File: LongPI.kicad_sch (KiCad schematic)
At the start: 10 parts, among them J1 USB_C_Receptacle_USB2.0, J2 Conn_01x30, U1 RP2040, U2 USBLC6-2SC6, U3 XC6210B332MR, U4 W25Q128JVS

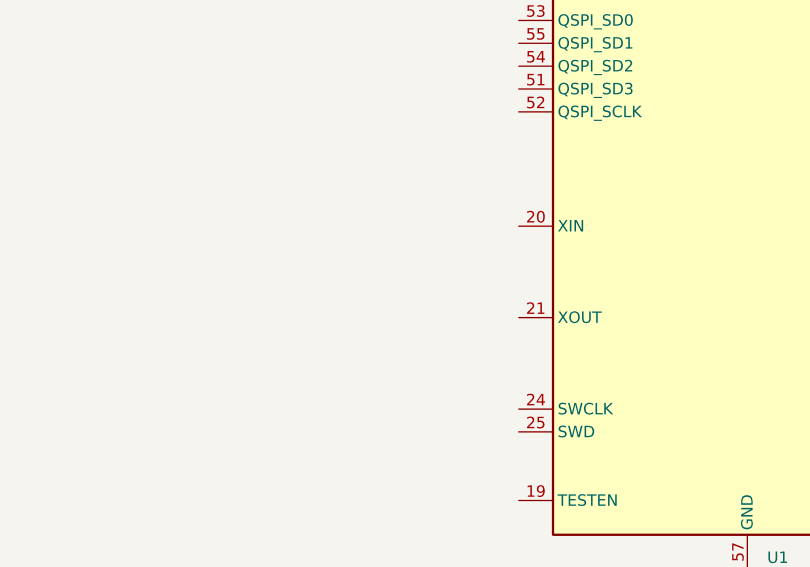
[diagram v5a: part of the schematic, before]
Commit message: Crystal setup on sch
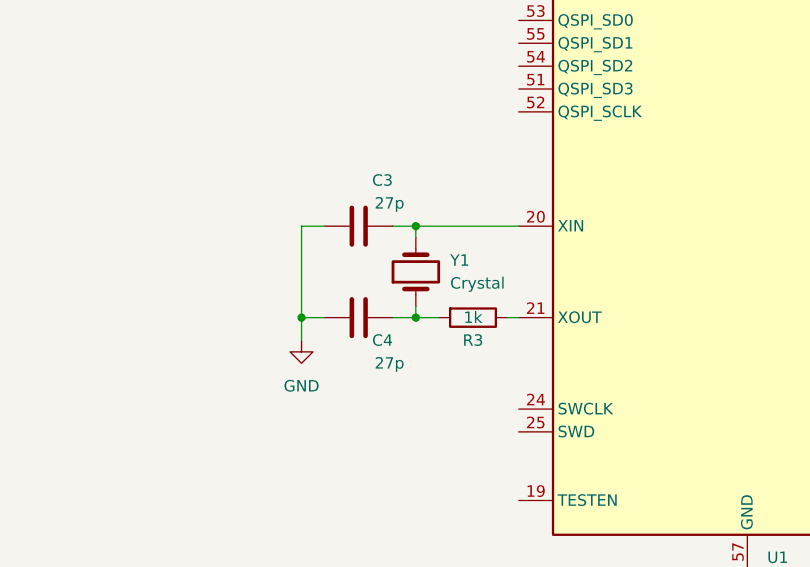
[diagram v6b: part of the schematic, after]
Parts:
- added C3, C4: 27p, symbol Device:C
- added R3: 1k, symbol Device:R
- added Y1: Crystal, symbol Device:Crystal
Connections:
- net GND: now also C3.1, C4.1
- net at U1.20 (XIN): now also C3.2, Y1.2
- net at U1.21 (XOUT): now also R3.1
- new net: C4.2, R3.2, Y1.1
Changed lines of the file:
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@@
   (junction (at 25.4 85.09) (diameter 0) (color 0 0 0 0)
   )
+  (junction (at 151.13 82.55) (diameter 0) (color 0 0 0 0)
+  )
   (junction (at 53.34 39.37) (diameter 0) (color 0 0 0 0)
   )
@@
   (junction (at 35.56 63.5) (diameter 0) (color 0 0 0 0)
   )
+  (junction (at 151.13 72.39) (diameter 0) (color 0 0 0 0)
+  )
   (junction (at 25.4 90.17) (diameter 0) (color 0 0 0 0)
   )
   (junction (at 53.34 85.09) (diameter 0) (color 0 0 0 0)
+  )
+  (junction (at 138.43 82.55) (diameter 0) (color 0 0 0 0)
   )
   (junction (at 93.98 121.92) (diameter 0) (color 0 0 0 0)
@@
     (stroke (width 0) (type default))
   )
+  (wire (pts (xy 138.43 72.39) (xy 138.43 82.55))
+    (stroke (width 0) (type default))
+  )
+  (wire (pts (xy 140.97 82.55) (xy 138.43 82.55))
+    (stroke (width 0) (type default))
+  )
   (wire (pts (xy 71.12 31.75) (xy 71.12 34.29))
     (stroke (width 0) (type default))
@@
     (stroke (width 0) (type default))
   )
+  (wire (pts (xy 151.13 82.55) (xy 151.13 81.28))
+    (stroke (width 0) (type default))
+  )
+  (wire (pts (xy 151.13 72.39) (xy 162.56 72.39))
+    (stroke (width 0) (type default))
+  )
   (wire (pts (xy 53.34 41.91) (xy 55.88 41.91))
     (stroke (width 0) (type default))
@@
     (stroke (width 0) (type default))
   )
+  (wire (pts (xy 148.59 72.39) (xy 151.13 72.39))
+    (stroke (width 0) (type default))
+  )
   (wire (pts (xy 39.37 97.79) (xy 39.37 100.33))
     (stroke (width 0) (type default))
@@
     (stroke (width 0) (type default))
   )
+  (wire (pts (xy 151.13 72.39) (xy 151.13 73.66))
+    (stroke (width 0) (type default))
+  )
   (wire (pts (xy 25.4 100.33) (xy 25.4 99.06))
     (stroke (width 0) (type default))
@@
     (stroke (width 0) (type default))
   )
+  (wire (pts (xy 138.43 82.55) (xy 138.43 85.09))
+    (stroke (width 0) (type default))
+  )
+  (wire (pts (xy 140.97 72.39) (xy 138.43 72.39))
+    (stroke (width 0) (type default))
+  )
   (wire (pts (xy 93.98 120.65) (xy 93.98 121.92))
     (stroke (width 0) (type default))
@@
     (stroke (width 0) (type default))
   )
+  (wire (pts (xy 148.59 82.55) (xy 151.13 82.55))
+    (stroke (width 0) (type default))
+  )
   (wire (pts (xy 53.34 39.37) (xy 55.88 39.37))
     (stroke (width 0) (type default))
@@
     (stroke (width 0) (type default))
   )
+  (wire (pts (xy 151.13 82.55) (xy 153.67 82.55))
+    (stroke (width 0) (type default))
+  )
   (wire (pts (xy 81.28 130.81) (xy 83.82 130.81))
     (stroke (width 0) (type default))
@@
   )
   (wire (pts (xy 25.4 100.33) (xy 39.37 100.33))
+    (stroke (width 0) (type default))
+  )
+  (wire (pts (xy 161.29 82.55) (xy 162.56 82.55))
     (stroke (width 0) (type default))
   )
@@
         (path "/cc33761c-f139-4a76-bdf7-f72d959ddb3d"
           (reference "#PWR09") (unit 1)
+        )
+      )
+    )
+  )
+  (symbol (lib_id "Device:Crystal") (at 151.13 77.47 90) (unit 1)
+    (in_bom yes) (on_board yes) (dnp no) (fields_autoplaced)
+    (property "Reference" "Y1" (at 154.94 76.2 90)
+      (effects (font (size 1.27 1.27)) (justify right))
+    )
+    (property "Value" "Crystal" (at 154.94 78.74 90)
+      (effects (font (size 1.27 1.27)) (justify right))
+    )
+    (property "Footprint" "" (at 151.13 77.47 0)
+      (effects (font (size 1.27 1.27)) hide)
+    )
+    (property "Datasheet" "~" (at 151.13 77.47 0)
+      (effects (font (size 1.27 1.27)) hide)
+    )
+    (pin "1")
+    (pin "2")
+    (instances
+      (project "LongPI"
+        (path "/cc33761c-f139-4a76-bdf7-f72d959ddb3d"
+          (reference "Y1") (unit 1)
         )
       )
@@
     )
   )
+  (symbol (lib_id "power:GND") (at 138.43 85.09 0) (unit 1)
+    (in_bom yes) (on_board yes) (dnp no) (fields_autoplaced)
+    (property "Reference" "#PWR011" (at 138.43 91.44 0)
+      (effects (font (size 1.27 1.27)) hide)
+    )
+    (property "Value" "GND" (at 138.43 90.17 0)
+      (effects (font (size 1.27 1.27)))
+    )
+    (property "Footprint" "" (at 138.43 85.09 0)
+      (effects (font (size 1.27 1.27)) hide)
+    )
+    (property "Datasheet" "" (at 138.43 85.09 0)
+      (effects (font (size 1.27 1.27)) hide)
+    )
+    (pin "1")
+    (instances
+      (project "LongPI"
+        (path "/cc33761c-f139-4a76-bdf7-f72d959ddb3d"
+          (reference "#PWR011") (unit 1)
+        )
+      )
+    )
+  )
   (symbol (lib_id "Connector:USB_C_Receptacle_USB2.0") (at 35.56 39.37 0) (unit 1)
     (in_bom yes) (on_board yes) (dnp no) (fields_autoplaced)
@@
         (path "/cc33761c-f139-4a76-bdf7-f72d959ddb3d"
           (reference "J1") (unit 1)
+        )
+      )
+    )
+  )
+  (symbol (lib_id "Device:C") (at 144.78 82.55 90) (unit 1)
+    (in_bom yes) (on_board yes) (dnp no)
+    (property "Reference" "C4" (at 148.59 85.09 90)
+      (effects (font (size 1.27 1.27)) (justify left))
+    )
+    (property "Value" "27p" (at 149.86 87.63 90)
+      (effects (font (size 1.27 1.27)) (justify left))
+    )
+    (property "Footprint" "" (at 148.59 81.5848 0)
+      (effects (font (size 1.27 1.27)) hide)
+    )
+    (property "Datasheet" "~" (at 144.78 82.55 0)
+      (effects (font (size 1.27 1.27)) hide)
+    )
+    (pin "1")
+    (pin "2")
+    (instances
+      (project "LongPI"
+        (path "/cc33761c-f139-4a76-bdf7-f72d959ddb3d"
+          (reference "C4") (unit 1)
+        )
+      )
+    )
+  )
+  (symbol (lib_id "Device:R") (at 157.48 82.55 270) (unit 1)
+    (in_bom yes) (on_board yes) (dnp no)
+    (property "Reference" "R3" (at 157.48 85.09 90)
+      (effects (font (size 1.27 1.27)))
+    )
+    (property "Value" "1k" (at 157.48 82.55 90)
+      (effects (font (size 1.27 1.27)))
+    )
+    (property "Footprint" "" (at 157.48 80.772 90)
+      (effects (font (size 1.27 1.27)) hide)
+    )
+    (property "Datasheet" "~" (at 157.48 82.55 0)
+      (effects (font (size 1.27 1.27)) hide)
+    )
+    (pin "1")
+    (pin "2")
+    (instances
+      (project "LongPI"
+        (path "/cc33761c-f139-4a76-bdf7-f72d959ddb3d"
+          (reference "R3") (unit 1)
         )
       )
@@
         )
       )
+    )
+  )
+  (symbol (lib_id "Device:C") (at 144.78 72.39 90) (unit 1)
+    (in_bom yes) (on_board yes) (dnp no)
+    (property "Reference" "C3" (at 148.59 67.31 90)
+      (effects (font (size 1.27 1.27)) (justify left))
+    )
+    (property "Value" "27p" (at 149.86 69.85 90)
+      (effects (font (size 1.27 1.27)) (justify left))
+    )
+    (property "Footprint" "" (at 148.59 71.4248 0)
+      (effects (font (size 1.27 1.27)) hide)
+    )
+    (property "Datasheet" "~" (at 144.78 72.39 0)
+      (effects (font (size 1.27 1.27)) hide)
+    )
+    (pin "1")
+    (pin "2")
+    (instances
+      (project "LongPI"
+        (path "/cc33761c-f139-4a76-bdf7-f72d959ddb3d"
+          (reference "C3") (unit 1)
+        )
+      )

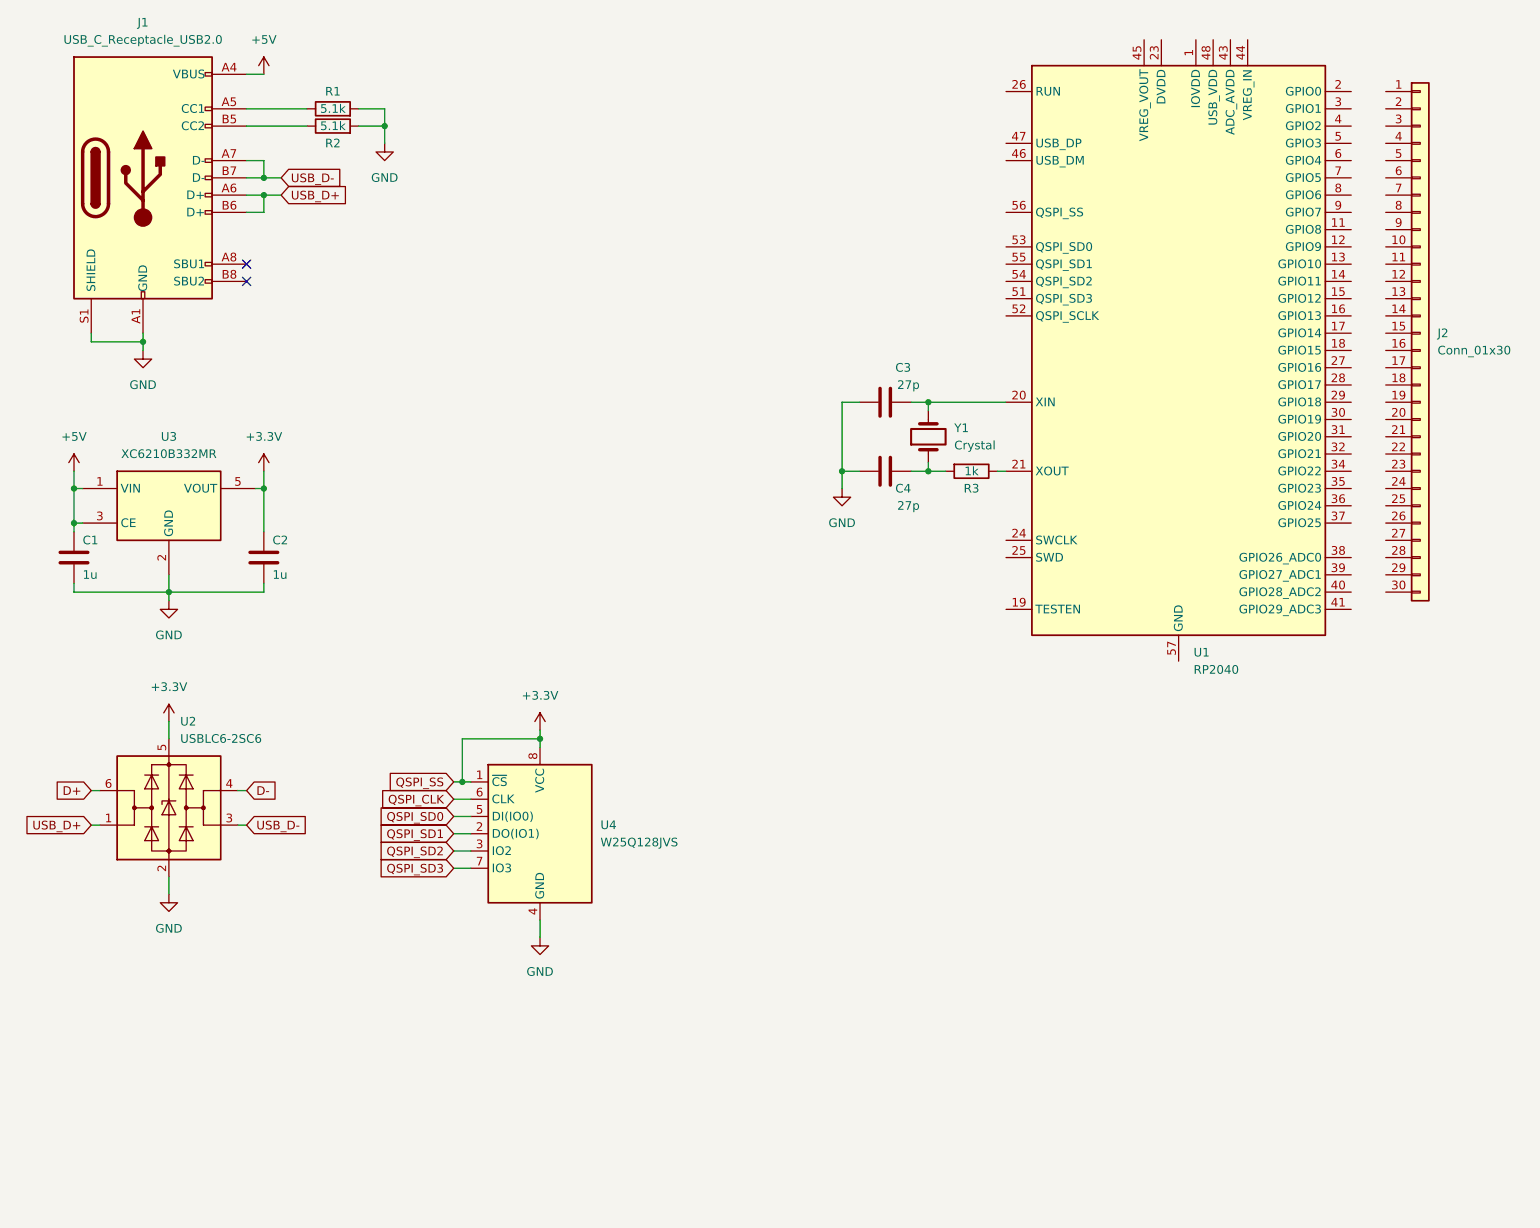
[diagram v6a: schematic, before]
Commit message: Decoupling capacitors setup on sch
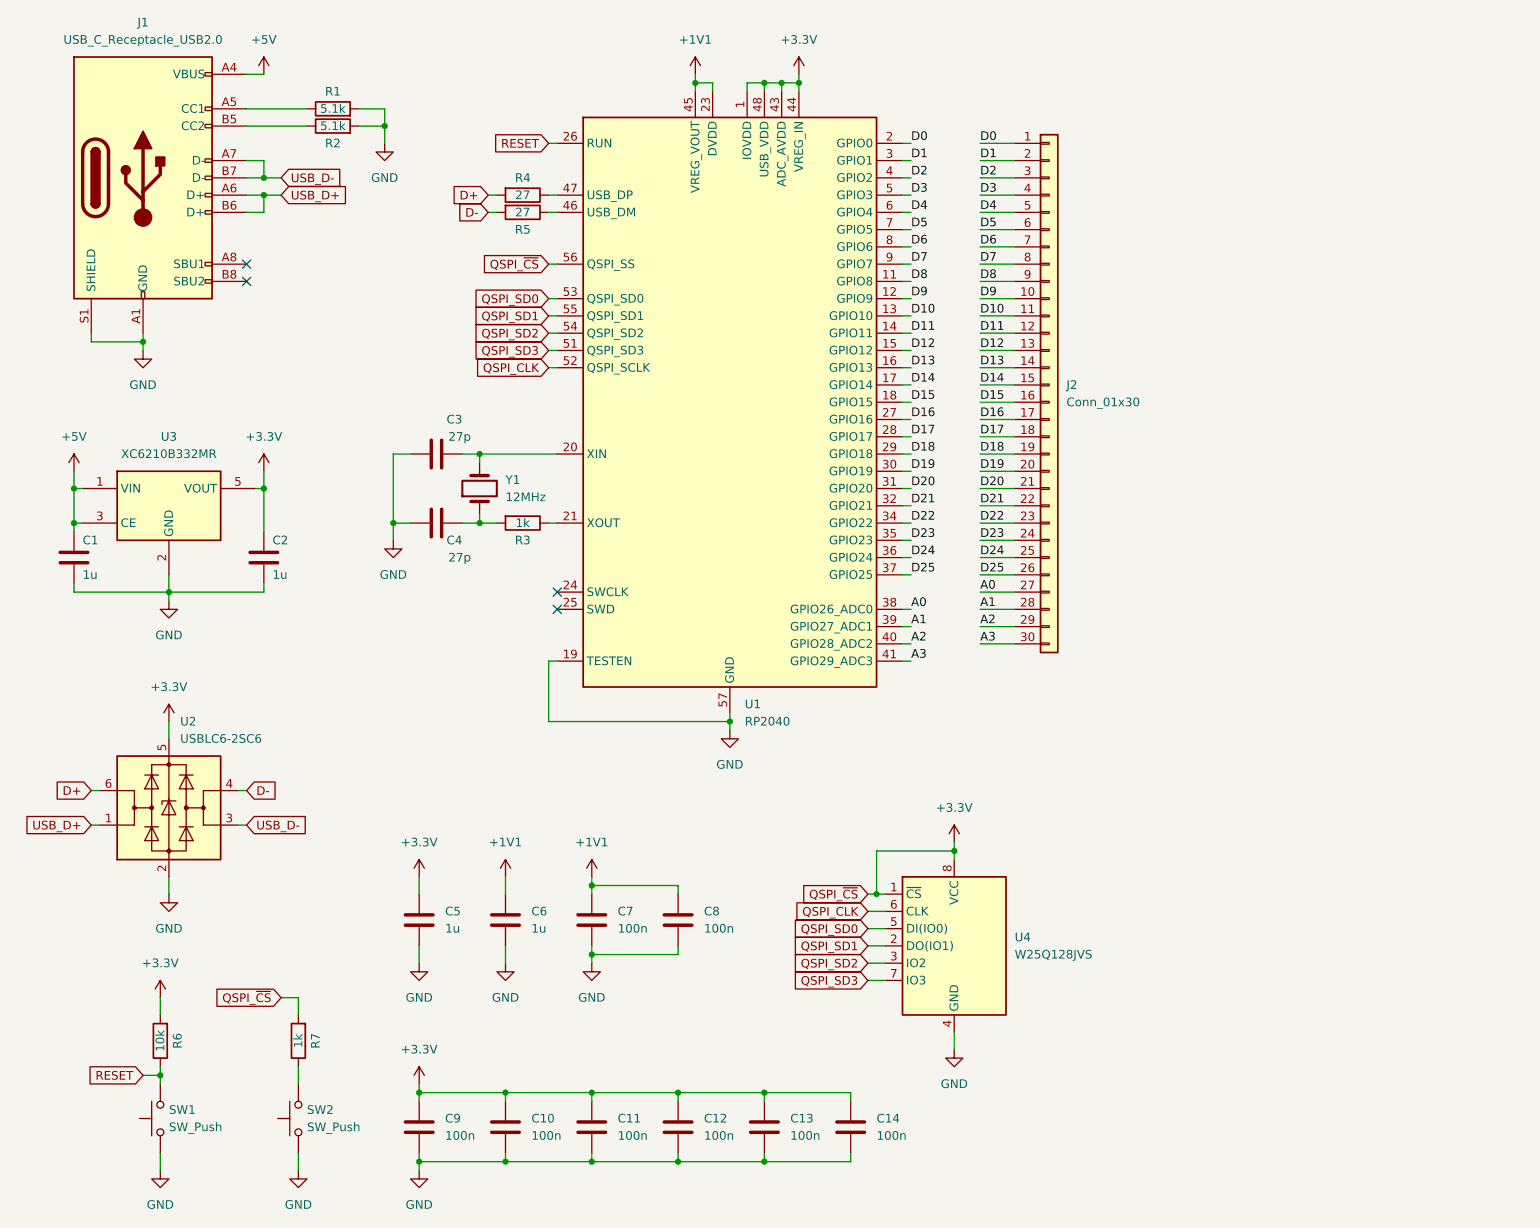
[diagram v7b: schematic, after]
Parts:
- added C10, C11, C12, C13, C14, C7, C8, C9: 100n, symbol Device:C
- added C5, C6: 1u, symbol Device:C
- added R4, R5: 27, symbol Device:R
- added R6: 10k, symbol Device:R
- added R7: 1k, symbol Device:R
- added SW1, SW2: SW_Push, symbol Switch:SW_Push
- Y1: value Crystal -> 12MHz
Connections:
- net +3.3V: now also U1.1 (IOVDD), U1.10 (IOVDD), U1.22 (IOVDD), U1.33 (IOVDD), U1.42 (IOVDD), U1.43 (ADC_AVDD), U1.44 (VREG_IN), U1.48 (USB_VDD), U1.49 (IOVDD), U1.56 (QSPI_SS), C10.1, C11.1, C12.1, C13.1, C14.1, C5.1, C9.1, R6.2, R7.2
- net D+: now also R4.2
- net D-: now also R5.2
- net GND: now also U1.19 (TESTEN), U1.57 (GND), C10.2, C11.2, C12.2, C13.2, C14.2, C5.2, C6.2, C7.2, C8.2, C9.2, SW1.1, SW2.1
- net QSPI_CLK: now also U1.52 (QSPI_SCLK)
- net QSPI_SD0: now also U1.53 (QSPI_SD0)
- net QSPI_SD1: now also U1.55 (QSPI_SD1)
- net QSPI_SD2: now also U1.54 (QSPI_SD2)
- net QSPI_SD3: now also U1.51 (QSPI_SD3)
- net D8: now reaches U1.11 (GPIO8)
- net D8: now also J2.9 (Pin_9)
- net D9: now reaches U1.12 (GPIO9)
- net D9: now also J2.10 (Pin_10)
- net D10: now reaches U1.13 (GPIO10)
- net D10: now also J2.11 (Pin_11)
- net D11: now reaches U1.14 (GPIO11)
- net D11: now also J2.12 (Pin_12)
- net D12: now reaches U1.15 (GPIO12)
- net D12: now also J2.13 (Pin_13)
- net D13: now reaches U1.16 (GPIO13)
- net D13: now also J2.14 (Pin_14)
- net D14: now reaches U1.17 (GPIO14)
- net D14: now also J2.15 (Pin_15)
- net D15: now reaches U1.18 (GPIO15)
- net D15: now also J2.16 (Pin_16)
- net D0: now reaches U1.2 (GPIO0)
- net D0: now also J2.1 (Pin_1)
- net +1V1: now reaches U1.23 (DVDD), U1.50 (DVDD)
- net +1V1: now also U1.45 (VREG_VOUT), C6.1, C7.1, C8.1
- net RESET: now reaches U1.26 (RUN)
- net RESET: now also R6.1, SW1.2
- net D16: now reaches U1.27 (GPIO16)
- net D16: now also J2.17 (Pin_17)
- net D17: now reaches U1.28 (GPIO17)
- net D17: now also J2.18 (Pin_18)
- net D18: now reaches U1.29 (GPIO18)
- net D18: now also J2.19 (Pin_19)
- net D1: now reaches U1.3 (GPIO1)
- net D1: now also J2.2 (Pin_2)
- net D19: now reaches U1.30 (GPIO19)
- net D19: now also J2.20 (Pin_20)
- net D20: now reaches U1.31 (GPIO20)
- net D20: now also J2.21 (Pin_21)
- net D21: now reaches U1.32 (GPIO21)
- net D21: now also J2.22 (Pin_22)
- net D22: now reaches U1.34 (GPIO22)
- net D22: now also J2.23 (Pin_23)
- net D23: now reaches U1.35 (GPIO23)
- net D23: now also J2.24 (Pin_24)
- net D24: now reaches U1.36 (GPIO24)
- net D24: now also J2.25 (Pin_25)
- net D25: now reaches U1.37 (GPIO25)
- net D25: now also J2.26 (Pin_26)
- net A0: now reaches U1.38 (GPIO26_ADC0)
- net A0: now also J2.27 (Pin_27)
- net A1: now reaches U1.39 (GPIO27_ADC1)
- net A1: now also J2.28 (Pin_28)
- net D2: now reaches U1.4 (GPIO2)
- net D2: now also J2.3 (Pin_3)
- net A2: now reaches U1.40 (GPIO28_ADC2)
- net A2: now also J2.29 (Pin_29)
- net A3: now reaches U1.41 (GPIO29_ADC3)
- net A3: now also J2.30 (Pin_30)
- net at U1.46 (USB_DM): now also R5.1
- net at U1.47 (USB_DP): now also R4.1
- net D3: now reaches U1.5 (GPIO3)
- net D3: now also J2.4 (Pin_4)
- net D4: now reaches U1.6 (GPIO4)
- net D4: now also J2.5 (Pin_5)
- net D5: now reaches U1.7 (GPIO5)
- net D5: now also J2.6 (Pin_6)
- net D6: now reaches U1.8 (GPIO6)
- net D6: now also J2.7 (Pin_7)
- net D7: now reaches U1.9 (GPIO7)
- net D7: now also J2.8 (Pin_8)
- new net: R7.1, SW2.2
- no-connect marks 2 -> 4
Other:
- moved on the sheet: C3, C4, J2, R3, U1, U4, Y1
